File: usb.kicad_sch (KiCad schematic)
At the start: 14 parts, among them J7 USB_C_Receptacle_USB2.0, U2 NCP606

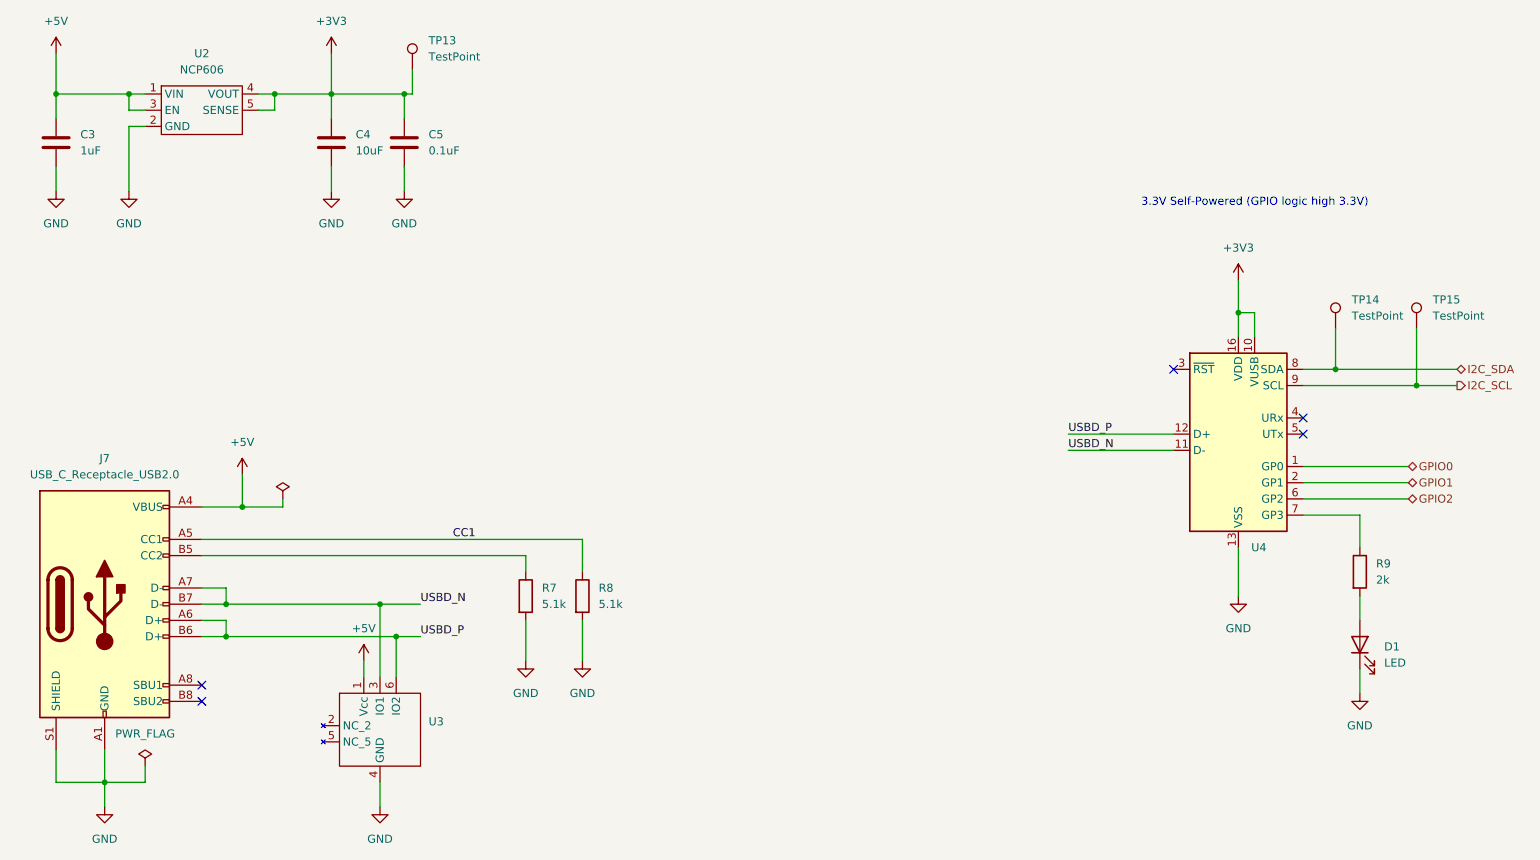
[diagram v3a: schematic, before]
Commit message: Associate built-in footprints
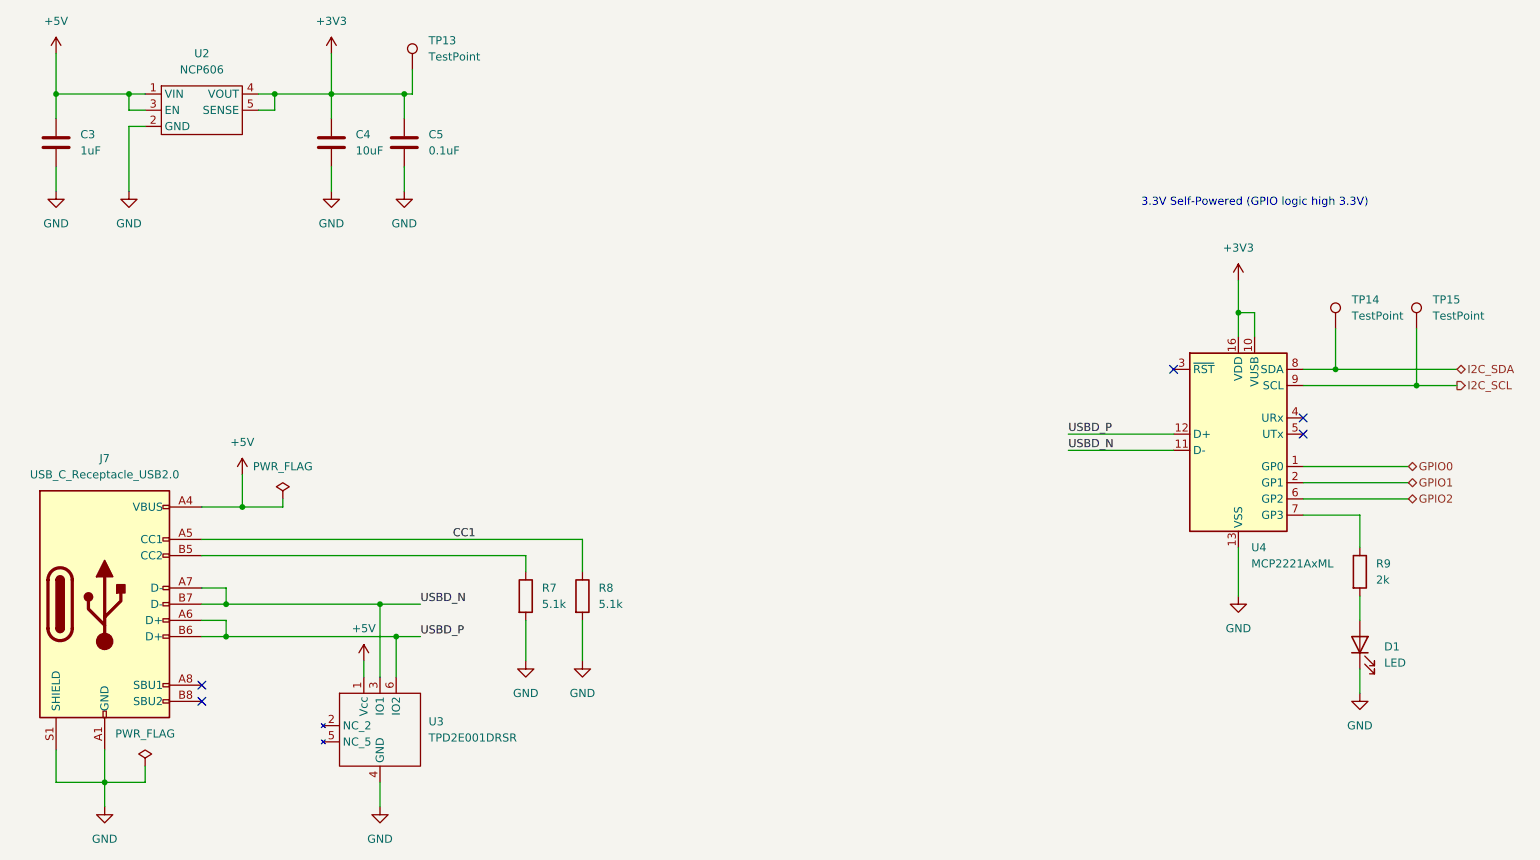
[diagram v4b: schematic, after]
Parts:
- C3: footprint (none) -> Capacitor_SMD:C_0603_1608Metric
- C4: footprint (none) -> Capacitor_SMD:C_0805_2012Metric
- C5: footprint (none) -> Capacitor_SMD:C_0402_1005Metric
- J7: footprint (none) -> Connector_USB:USB_C_Receptacle_GCT_USB4085
- R7, R8, R9: footprint (none) -> Resistor_SMD:R_0402_1005Metric
- TP13, TP14, TP15: footprint (none) -> TestPoint:TestPoint_Pad_D2.0mm
- U3: value (none) -> TPD2E001DRSR
- U4: value ~ -> MCP2221AxML; footprint (none) -> Package_DFN_QFN:QFN-16-1EP_4x4mm_P0.65mm_EP2.5x2.5mm
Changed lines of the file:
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@@
     (property "Reference" "J7" (id 0) (at 39.37 119.38 0))
     (property "Value" "USB_C_Receptacle_USB2.0" (id 1) (at 39.37 121.92 0))
-    (property "Footprint" "" (id 2) (at 43.18 142.24 0)
+    (property "Footprint" "Connector_USB:USB_C_Receptacle_GCT_USB4085" (id 2) (at 43.18 142.24 0)
       (effects (font (size 1.27 1.27)) hide)
     )
@@
       (effects (font (size 1.27 1.27)) hide)
     )
-    (property "Value" "" (id 1) (at 67.31 120.65 0))
+    (property "Value" "PWR_FLAG" (id 1) (at 67.31 120.65 0))
     (property "Footprint" "" (id 2) (at 67.31 125.73 0)
       (effects (font (size 1.27 1.27)) hide)
@@
       (effects (font (size 1.27 1.27)) (justify left))
     )
-    (property "Value" "" (id 1) (at 90.17 163.1949 0)
+    (property "Value" "TPD2E001DRSR" (id 1) (at 90.17 163.1949 0)
       (effects (font (size 1.27 1.27)) (justify left))
     )
@@
       (effects (font (size 1.27 1.27)) (justify left))
     )
-    (property "Footprint" "" (id 2) (at 32.7152 73.66 0)
+    (property "Footprint" "Capacitor_SMD:C_0603_1608Metric" (id 2) (at 32.7152 73.66 0)
       (effects (font (size 1.27 1.27)) hide)
     )
@@
       (effects (font (size 1.27 1.27)) (justify left))
     )
-    (property "Footprint" "" (id 2) (at 87.3252 73.66 0)
+    (property "Footprint" "Capacitor_SMD:C_0402_1005Metric" (id 2) (at 87.3252 73.66 0)
       (effects (font (size 1.27 1.27)) hide)
     )
@@
       (effects (font (size 1.27 1.27)) (justify left))
     )
-    (property "Footprint" "" (id 2) (at 92.71 58.42 0)
+    (property "Footprint" "TestPoint:TestPoint_Pad_D2.0mm" (id 2) (at 92.71 58.42 0)
       (effects (font (size 1.27 1.27)) hide)
     )
@@
       (effects (font (size 1.27 1.27)) (justify left))
     )
-    (property "Footprint" "" (id 2) (at 234.442 137.16 90)
+    (property "Footprint" "Resistor_SMD:R_0402_1005Metric" (id 2) (at 234.442 137.16 90)
       (effects (font (size 1.27 1.27)) hide)
     )
@@
       (effects (font (size 1.27 1.27)) (justify left))
     )
-    (property "Footprint" "" (id 2) (at 112.522 140.97 90)
+    (property "Footprint" "Resistor_SMD:R_0402_1005Metric" (id 2) (at 112.522 140.97 90)
       (effects (font (size 1.27 1.27)) hide)
     )
@@
       (effects (font (size 1.27 1.27)) (justify left))
     )
-    (property "Footprint" "" (id 2) (at 250.19 99.06 0)
+    (property "Footprint" "TestPoint:TestPoint_Pad_D2.0mm" (id 2) (at 250.19 99.06 0)
       (effects (font (size 1.27 1.27)) hide)
     )
@@
       (effects (font (size 1.27 1.27)) (justify left))
     )
-    (property "Value" "~" (id 1) (at 219.1894 135.89 0)
-      (effects (font (size 1.27 1.27)) (justify left))
-    )
-    (property "Footprint" "" (id 2) (at 217.17 92.71 0)
+    (property "Value" "MCP2221AxML" (id 1) (at 219.1894 135.89 0)
+      (effects (font (size 1.27 1.27)) (justify left))
+    )
+    (property "Footprint" "Package_DFN_QFN:QFN-16-1EP_4x4mm_P0.65mm_EP2.5x2.5mm" (id 2) (at 217.17 92.71 0)
       (effects (font (size 1.27 1.27)) hide)
     )
@@
       (effects (font (size 1.27 1.27)) (justify left))
     )
-    (property "Footprint" "" (id 2) (at 75.8952 73.66 0)
+    (property "Footprint" "Capacitor_SMD:C_0805_2012Metric" (id 2) (at 75.8952 73.66 0)
       (effects (font (size 1.27 1.27)) hide)
     )
@@
       (effects (font (size 1.27 1.27)) (justify left))
     )
-    (property "Footprint" "" (id 2) (at 103.632 140.97 90)
+    (property "Footprint" "Resistor_SMD:R_0402_1005Metric" (id 2) (at 103.632 140.97 90)
       (effects (font (size 1.27 1.27)) hide)
     )
@@
       (effects (font (size 1.27 1.27)) (justify left))
     )
-    (property "Footprint" "" (id 2) (at 237.49 99.06 0)
-      (effects (font (size 1.27 1.27)) hide)
-    )
+    (property "Footprint" "TestPoint:TestPoint_Pad_D2.0mm" (id 2) (at 237.49 99.06 0)
+      (effects (font (size 1.27 1.27)) hide)
+    )

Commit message: Add part number fields in schematic
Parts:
- C3, C4, C5, R7, R8, R9: MfgPartNo (none) -> GENERIC
- D1: Manufacturer (none) -> Wurth; MfgPartNo (none) -> 150060VS55040; Vendor (none) -> Digi-Key; VendorPartNo (none) -> 732-12017-1-ND
- J7: Manufacturer (none) -> GCT; MfgPartNo (none) -> USB4085-GF-A; Vendor (none) -> Digi-Key; VendorPartNo (none) -> 2073-USB4085-GF-ACT-ND
- U2: Manufacturer (none) -> Onsemi; MfgPartNo (none) -> NCP606MN33T2G; Vendor (none) -> Digi-Key; VendorPartNo (none) -> NCP606MN33T2GOSCT-ND
- U3: Manufacturer (none) -> Texas Instruments; MfgPartNo (none) -> TPD2E001DRSR; Vendor (none) -> Digi-Key; VendorPartNo (none) -> 296-22850-1-ND
- U4: Manufacturer (none) -> Microchip; MfgPartNo (none) -> MCP2221A-I/ML; Vendor (none) -> Digi-Key; VendorPartNo (none) -> MCP2221A-I/ML-ND
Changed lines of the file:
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@@
       (effects (font (size 1.27 1.27)) hide)
+    )
+    (property "Vendor" "Digi-Key" (id 4) (at 240.03 159.0674 90)
+      (effects (font (size 1.27 1.27)) (justify right) hide)
+    )
+    (property "VendorPartNo" "732-12017-1-ND" (id 5) (at 240.03 161.6074 90)
+      (effects (font (size 1.27 1.27)) (justify right) hide)
+    )
+    (property "Manufacturer" "Wurth" (id 6) (at 240.03 164.1474 90)
+      (effects (font (size 1.27 1.27)) (justify right) hide)
+    )
+    (property "MfgPartNo" "150060VS55040" (id 7) (at 240.03 166.6874 90)
+      (effects (font (size 1.27 1.27)) (justify right) hide)
     )
     (pin "1")
@@
     )
     (property "Datasheet" "https://www.usb.org/sites/default/files/documents/usb_type-c.zip" (id 3) (at 43.18 142.24 0)
+      (effects (font (size 1.27 1.27)) hide)
+    )
+    (property "Vendor" "Digi-Key" (id 4) (at 39.37 129.54 0)
+      (effects (font (size 1.27 1.27)) hide)
+    )
+    (property "VendorPartNo" "2073-USB4085-GF-ACT-ND" (id 5) (at 39.37 132.08 0)
+      (effects (font (size 1.27 1.27)) hide)
+    )
+    (property "Manufacturer" "GCT" (id 6) (at 39.37 134.62 0)
+      (effects (font (size 1.27 1.27)) hide)
+    )
+    (property "MfgPartNo" "USB4085-GF-A" (id 7) (at 39.37 137.16 0)
       (effects (font (size 1.27 1.27)) hide)
     )
@@
       (effects (font (size 1.27 1.27)) hide)
     )
+    (property "Vendor" "Digi-Key" (id 4) (at 90.17 170.8149 0)
+      (effects (font (size 1.27 1.27)) (justify left) hide)
+    )
+    (property "VendorPartNo" "296-22850-1-ND" (id 5) (at 90.17 173.3549 0)
+      (effects (font (size 1.27 1.27)) (justify left) hide)
+    )
+    (property "Manufacturer" "Texas Instruments" (id 6) (at 90.17 175.8949 0)
+      (effects (font (size 1.27 1.27)) (justify left) hide)
+    )
+    (property "MfgPartNo" "TPD2E001DRSR" (id 7) (at 90.17 178.4349 0)
+      (effects (font (size 1.27 1.27)) (justify left) hide)
+    )
     (pin "1")
     (pin "2")
@@
       (effects (font (size 1.27 1.27)) hide)
     )
+    (property "Vendor" "~" (id 4) (at 35.56 78.7399 0)
+      (effects (font (size 1.27 1.27)) (justify left) hide)
+    )
+    (property "VendorPartNo" "~" (id 5) (at 35.56 81.2799 0)
+      (effects (font (size 1.27 1.27)) (justify left) hide)
+    )
+    (property "MfgPartNo" "GENERIC" (id 6) (at 35.56 83.8199 0)
+      (effects (font (size 1.27 1.27)) (justify left) hide)
+    )
     (pin "1")
     (pin "2")
@@
       (effects (font (size 1.27 1.27)) hide)
     )
+    (property "Vendor" "~" (id 4) (at 90.17 78.7399 0)
+      (effects (font (size 1.27 1.27)) (justify left) hide)
+    )
+    (property "VendorPartNo" "~" (id 5) (at 90.17 81.2799 0)
+      (effects (font (size 1.27 1.27)) (justify left) hide)
+    )
+    (property "MfgPartNo" "GENERIC" (id 6) (at 90.17 83.8199 0)
+      (effects (font (size 1.27 1.27)) (justify left) hide)
+    )
     (pin "1")
     (pin "2")
@@
       (effects (font (size 1.27 1.27)) hide)
     )
+    (property "Vendor" "~" (id 4) (at 90.17 64.0079 0)
+      (effects (font (size 1.27 1.27)) (justify left) hide)
+    )
+    (property "VendorPartNo" "~" (id 5) (at 90.17 66.5479 0)
+      (effects (font (size 1.27 1.27)) (justify left) hide)
+    )
+    (property "MfgPartNo" "~" (id 6) (at 90.17 69.0879 0)
+      (effects (font (size 1.27 1.27)) (justify left) hide)
+    )
     (pin "1")
   )
@@
     (property "Datasheet" "~" (id 3) (at 236.22 137.16 0)
       (effects (font (size 1.27 1.27)) hide)
+    )
+    (property "Vendor" "~" (id 4) (at 238.76 146.0499 0)
+      (effects (font (size 1.27 1.27)) (justify left) hide)
+    )
+    (property "VendorPartNo" "~" (id 5) (at 238.76 148.5899 0)
+      (effects (font (size 1.27 1.27)) (justify left) hide)
+    )
+    (property "MfgPartNo" "GENERIC" (id 6) (at 238.76 151.1299 0)
+      (effects (font (size 1.27 1.27)) (justify left) hide)
     )
     (pin "1")
@@
     )
     (property "Datasheet" "" (id 3) (at 52.07 64.77 0)
+      (effects (font (size 1.27 1.27)) hide)
+    )
+    (property "Vendor" "Digi-Key" (id 4) (at 54.61 66.04 0)
+      (effects (font (size 1.27 1.27)) hide)
+    )
+    (property "VendorPartNo" "NCP606MN33T2GOSCT-ND" (id 5) (at 54.61 68.58 0)
+      (effects (font (size 1.27 1.27)) hide)
+    )
+    (property "Manufacturer" "Onsemi" (id 6) (at 54.61 71.12 0)
+      (effects (font (size 1.27 1.27)) hide)
+    )
+    (property "MfgPartNo" "NCP606MN33T2G" (id 7) (at 54.61 73.66 0)
       (effects (font (size 1.27 1.27)) hide)
     )
@@
       (effects (font (size 1.27 1.27)) hide)
     )
+    (property "Vendor" "~" (id 4) (at 116.84 149.8599 0)
+      (effects (font (size 1.27 1.27)) (justify left) hide)
+    )
+    (property "VendorPartNo" "~" (id 5) (at 116.84 152.3999 0)
+      (effects (font (size 1.27 1.27)) (justify left) hide)
+    )
+    (property "MfgPartNo" "GENERIC" (id 6) (at 116.84 154.9399 0)
+      (effects (font (size 1.27 1.27)) (justify left) hide)
+    )
     (pin "1")
     (pin "2")
@@
     (property "Datasheet" "~" (id 3) (at 250.19 99.06 0)
       (effects (font (size 1.27 1.27)) hide)
+    )
+    (property "Vendor" "~" (id 4) (at 247.65 104.6479 0)
+      (effects (font (size 1.27 1.27)) (justify left) hide)
+    )
+    (property "VendorPartNo" "~" (id 5) (at 247.65 107.1879 0)
+      (effects (font (size 1.27 1.27)) (justify left) hide)
+    )
+    (property "MfgPartNo" "~" (id 6) (at 247.65 109.7279 0)
+      (effects (font (size 1.27 1.27)) (justify left) hide)
     )
     (pin "1")
@@
     (property "Datasheet" "http://ww1.microchip.com/downloads/en/DeviceDoc/20005565B.pdf" (id 3) (at 217.17 100.33 0)
       (effects (font (size 1.27 1.27)) hide)
+    )
+    (property "Vendor" "Digi-Key" (id 4) (at 219.1894 143.51 0)
+      (effects (font (size 1.27 1.27)) (justify left) hide)
+    )
+    (property "VendorPartNo" "MCP2221A-I/ML-ND" (id 5) (at 219.1894 146.05 0)
+      (effects (font (size 1.27 1.27)) (justify left) hide)
+    )
+    (property "Manufacturer" "Microchip" (id 6) (at 219.1894 148.59 0)
+      (effects (font (size 1.27 1.27)) (justify left) hide)
+    )
+    (property "MfgPartNo" "MCP2221A-I/ML" (id 7) (at 219.1894 151.13 0)
+      (effects (font (size 1.27 1.27)) (justify left) hide)
     )
     (pin "1")
@@
       (effects (font (size 1.27 1.27)) hide)
     )
+    (property "Vendor" "~" (id 4) (at 78.74 78.7399 0)
+      (effects (font (size 1.27 1.27)) (justify left) hide)
+    )
+    (property "VendorPartNo" "~" (id 5) (at 78.74 81.2799 0)
+      (effects (font (size 1.27 1.27)) (justify left) hide)
+    )
+    (property "MfgPartNo" "GENERIC" (id 6) (at 78.74 83.8199 0)
+      (effects (font (size 1.27 1.27)) (justify left) hide)
+    )
     (pin "1")
     (pin "2")
@@
     (property "Datasheet" "~" (id 3) (at 105.41 140.97 0)
       (effects (font (size 1.27 1.27)) hide)
+    )
+    (property "Vendor" "~" (id 4) (at 107.95 149.8599 0)
+      (effects (font (size 1.27 1.27)) (justify left) hide)
+    )
+    (property "VendorPartNo" "~" (id 5) (at 107.95 152.3999 0)
+      (effects (font (size 1.27 1.27)) (justify left) hide)
+    )
+    (property "MfgPartNo" "GENERIC" (id 6) (at 107.95 154.9399 0)
+      (effects (font (size 1.27 1.27)) (justify left) hide)
     )
     (pin "1")
@@
       (effects (font (size 1.27 1.27)) hide)
     )
-    (pin "1")
+    (property "Vendor" "~" (id 4) (at 234.95 104.6479 0)
+      (effects (font (size 1.27 1.27)) (justify left) hide)
+    )
+    (property "VendorPartNo" "~" (id 5) (at 234.95 107.1879 0)
+      (effects (font (size 1.27 1.27)) (justify left) hide)
+    )
+    (property "MfgPartNo" "~" (id 6) (at 234.95 109.7279 0)
+      (effects (font (size 1.27 1.27)) (justify left) hide)
+    )
+    (pin "1")

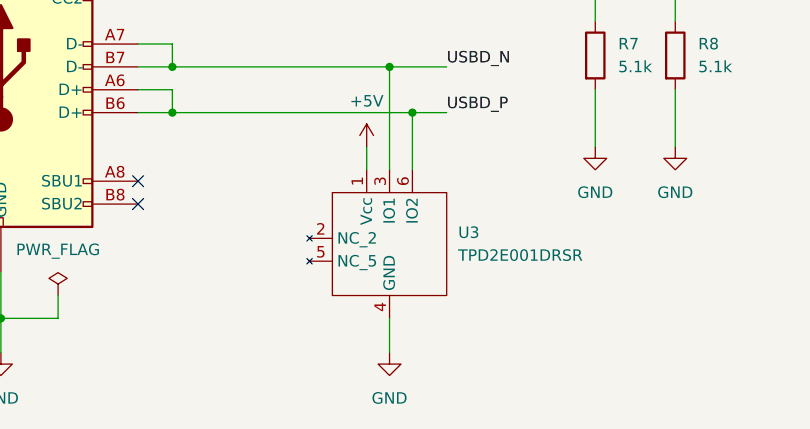
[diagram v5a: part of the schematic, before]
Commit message: Associate LED footprint; create/associate TVS diode footprint
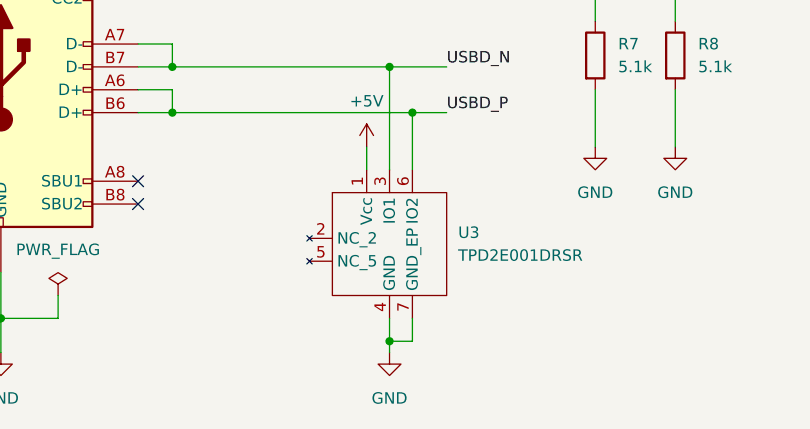
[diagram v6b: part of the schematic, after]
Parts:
- D1: footprint (none) -> LED_SMD:LED_0603_1608Metric
- U3: footprint (none) -> toast:SON7P95_300X300X80L50X35T190X120N
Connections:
- net GND: now also U3.7 (GND_EP)
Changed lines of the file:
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@@
   (junction (at 217.17 96.52) (diameter 0) (color 0 0 0 0)
+  )
+  (junction (at 82.55 172.72) (diameter 0) (color 0 0 0 0)
   )
   (junction (at 232.41 105.41) (diameter 0) (color 0 0 0 0)
@@
     (stroke (width 0) (type default) (color 0 0 0 0))
   )
+  (wire (pts (xy 85.09 172.72) (xy 82.55 172.72))
+    (stroke (width 0) (type default) (color 0 0 0 0))
+  )
   (wire (pts (xy 74.93 73.66) (xy 74.93 77.47))
     (stroke (width 0) (type default) (color 0 0 0 0))
@@
     (stroke (width 0) (type default) (color 0 0 0 0))
   )
-  (wire (pts (xy 82.55 170.18) (xy 82.55 173.99))
+  (wire (pts (xy 82.55 170.18) (xy 82.55 172.72))
     (stroke (width 0) (type default) (color 0 0 0 0))
   )
@@
     (stroke (width 0) (type default) (color 0 0 0 0))
   )
+  (wire (pts (xy 85.09 170.18) (xy 85.09 172.72))
+    (stroke (width 0) (type default) (color 0 0 0 0))
+  )
   (wire (pts (xy 245.11 107.95) (xy 251.46 107.95))
     (stroke (width 0) (type default) (color 0 0 0 0))
   )
   (wire (pts (xy 82.55 142.24) (xy 88.9 142.24))
+    (stroke (width 0) (type default) (color 0 0 0 0))
+  )
+  (wire (pts (xy 82.55 172.72) (xy 82.55 173.99))
     (stroke (width 0) (type default) (color 0 0 0 0))
   )
@@
       (effects (font (size 1.27 1.27)) (justify right))
     )
-    (property "Footprint" "" (id 2) (at 236.22 148.59 0)
+    (property "Footprint" "LED_SMD:LED_0603_1608Metric" (id 2) (at 236.22 148.59 0)
       (effects (font (size 1.27 1.27)) hide)
     )
@@
       (effects (font (size 1.27 1.27)) (justify left))
     )
-    (property "Footprint" "" (id 2) (at 76.2 161.29 0)
+    (property "Footprint" "toast:SON7P95_300X300X80L50X35T190X120N" (id 2) (at 76.2 161.29 0)
       (effects (font (size 1.27 1.27)) hide)
     )
@@
       (effects (font (size 1.27 1.27)) (justify left) hide)
     )
+    (pin "7")
     (pin "1")
     (pin "2")

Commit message: NCP606 footprint
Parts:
- U2: footprint (none) -> toast:SON7P95_300X330X100L50X35T200X120N
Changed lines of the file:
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@@
     (property "Reference" "U2" (id 0) (at 54.61 55.88 0))
     (property "Value" "NCP606" (id 1) (at 54.61 58.42 0))
-    (property "Footprint" "" (id 2) (at 52.07 64.77 0)
+    (property "Footprint" "toast:SON7P95_300X330X100L50X35T200X120N" (id 2) (at 52.07 64.77 0)
       (effects (font (size 1.27 1.27)) hide)
     )
